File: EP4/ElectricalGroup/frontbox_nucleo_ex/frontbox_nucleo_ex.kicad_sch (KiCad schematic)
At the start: 1 part, among them U1 NUCLEOH723ZG_WITHOUT_MORHPHO

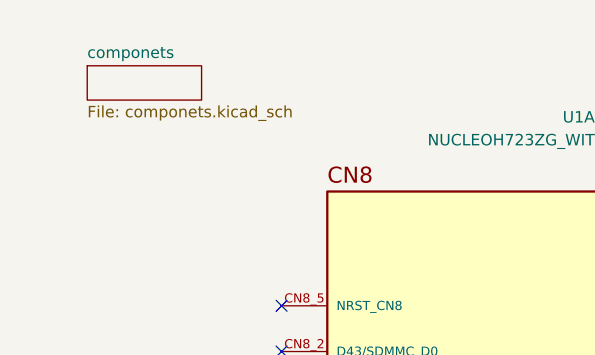
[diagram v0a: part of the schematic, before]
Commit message: rename components schematic sheet
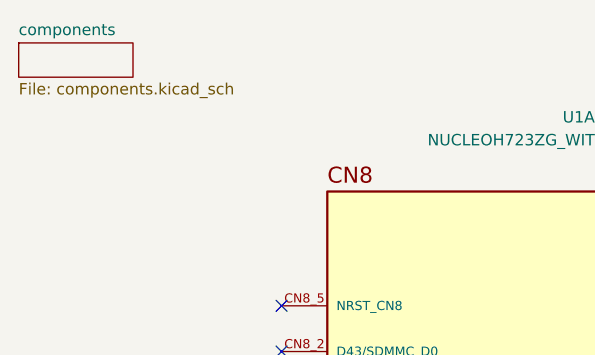
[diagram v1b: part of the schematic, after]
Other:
- removed sheet componets
- added sheet components (components.kicad_sch)
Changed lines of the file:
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@@
     )
   )
-  (sheet (at 27.305 22.225) (size 12.7 3.81) (fields_autoplaced)
+  (sheet (at 19.685 19.685) (size 12.7 3.81) (fields_autoplaced)
     (stroke (width 0.1524) (type solid))
     (fill (color 0 0 0 0.0000))
-    (property "Sheetname" "componets" (at 27.305 21.5134 0)
+    (property "Sheetname" "components" (at 19.685 18.9734 0)
       (effects (font (size 1.27 1.27)) (justify left bottom))
     )
-    (property "Sheetfile" "componets.kicad_sch" (at 27.305 26.6196 0)
+    (property "Sheetfile" "components.kicad_sch" (at 19.685 24.0796 0)
       (effects (font (size 1.27 1.27)) (justify left top))
     )
